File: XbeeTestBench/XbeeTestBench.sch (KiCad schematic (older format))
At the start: 7 parts, among them J1 Conn_01x02, J2 Conn_01x06, J3 Conn_01x15, J4 Conn_01x15, U1 Xbee802.15.4

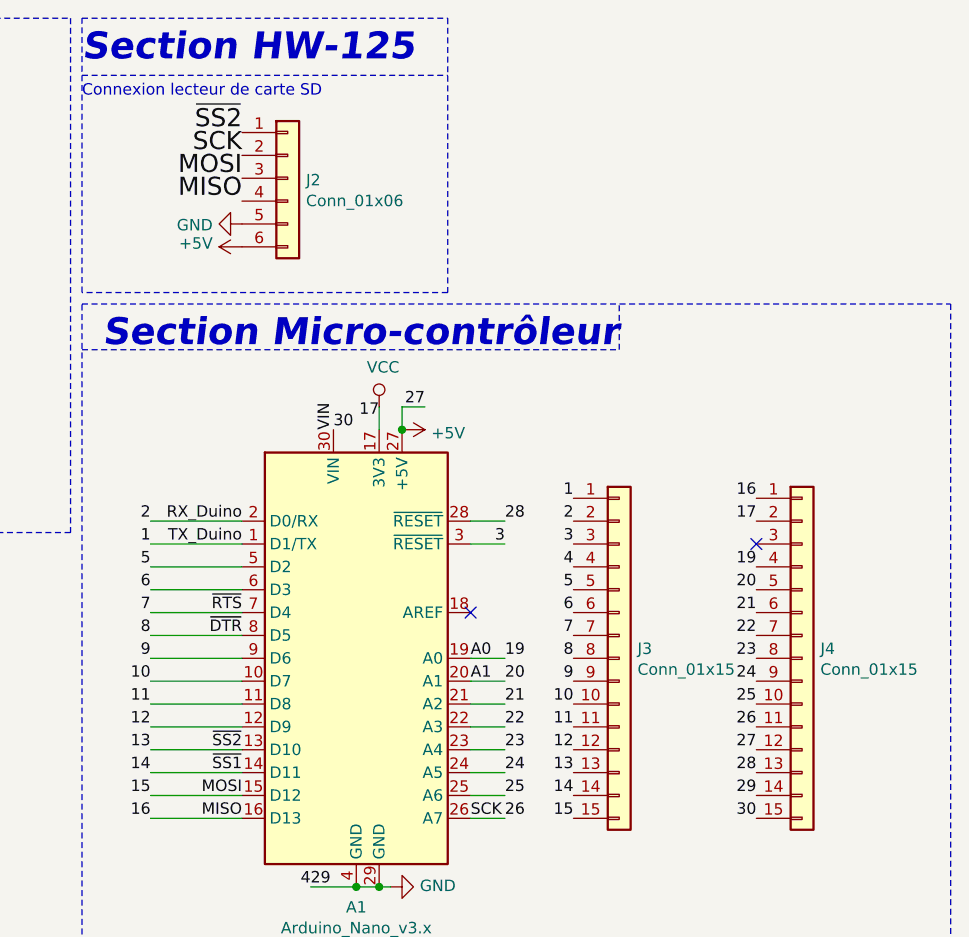
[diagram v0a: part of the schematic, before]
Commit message: Mise à jour + PDF Banc Xbee
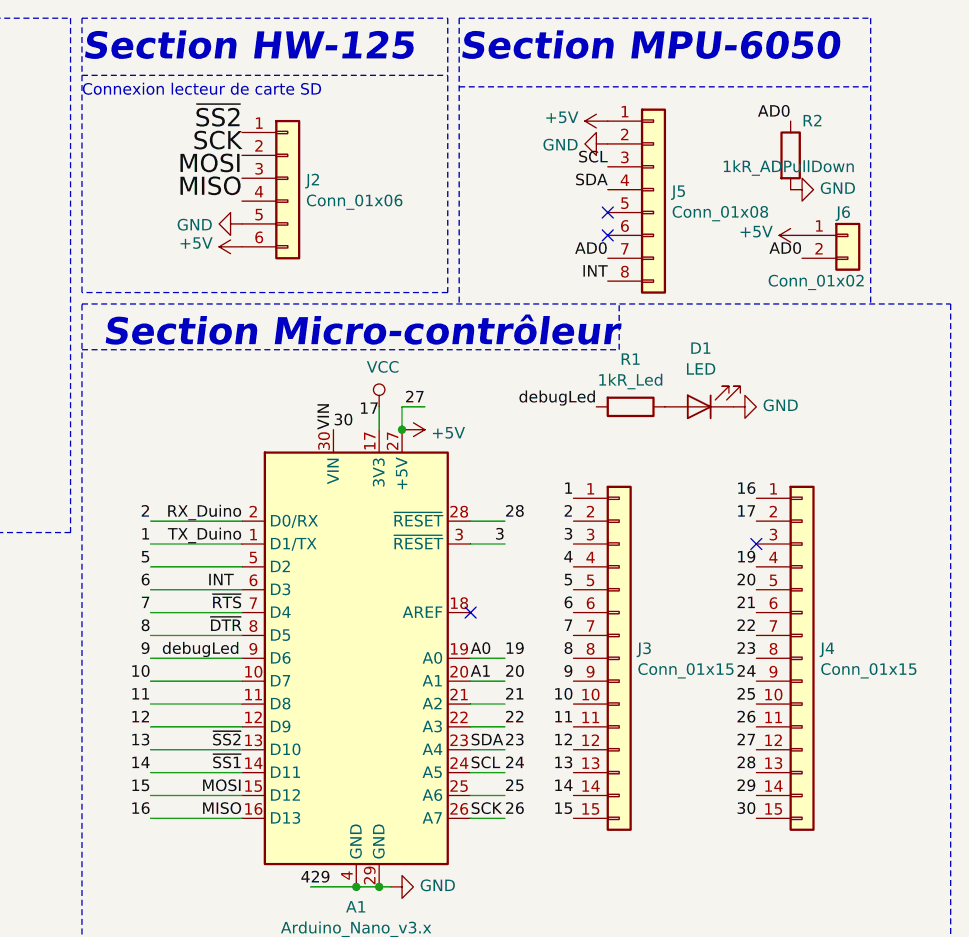
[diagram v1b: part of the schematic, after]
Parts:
- added D1: LED, LED_THT:LED_D5.0mm, symbol Device:LED
- added J5: Conn_01x08, Connector_PinSocket_2.54mm:PinSocket_1x08_P2.54mm_Vertical, symbol Connector_Generic:Conn_01x08
- added J6: Conn_01x02, Connector_PinSocket_2.54mm:PinSocket_1x02_P2.54mm_Horizontal, symbol Connector_Generic:Conn_01x02
- added R1: 1kR_Led, Resistor_SMD:R_1206_3216Metric_Pad1.42x1.75mm_HandSolder, symbol Device:R
- added R2: 1kR_ADPullDown, Resistor_SMD:R_1206_3216Metric_Pad1.42x1.75mm_HandSolder, symbol Device:R
- J1: footprint Connector_PinHeader_2.54mm:PinHeader_1x02_P2.54mm_Vertical -> rex:BatConn
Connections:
- net +5V: now also J5.1 (Pin_1), J6.1 (Pin_1)
- net 23: now also J5.4 (Pin_4)
- net 24: now also J5.3 (Pin_3)
- net 6: now also J5.8 (Pin_8)
- net 9: now also R1.2
- net GND: now also D1.1 (K), J5.2 (Pin_2), R2.2
- new net: D1.2 (A), R1.1
- new net AD0: J5.7 (Pin_7), J6.2 (Pin_2), R2.1
- no-connect marks 10 -> 12
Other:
- note added: "Section MPU-6050\n"
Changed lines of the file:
@@
 F 0 "J1" H 1480 3392 50  0000 L CNN
 F 1 "Conn_01x02" H 1480 3301 50  0000 L CNN
-F 2 "Connector_PinHeader_2.54mm:PinHeader_1x02_P2.54mm_Vertical" H 1400 3400 50  0001 C CNN
+F 2 "rex:BatConn" H 1400 3400 50  0001 C CNN
 F 3 "~" H 1400 3400 50  0001 C CNN
 	1    1400 3400
@@
 Wire Notes Line
 	3150 4550 3150 1750
-Wire Notes Line
-	3150 1750 6950 1750
 Text Notes 5500 1950 2    118  Italic 24
 Section Micro-contrôleur
@@
 	1    0    0    -1
 $EndComp
+$Comp
+L Connector_Generic:Conn_01x08 J5
+U 1 1 5DEA7475
+P 5650 1250
+F 0 "J5" H 5730 1242 50  0000 L CNN
+F 1 "Conn_01x08" H 5730 1151 50  0000 L CNN
+F 2 "Connector_PinSocket_2.54mm:PinSocket_1x08_P2.54mm_Vertical" H 5650 1250 50  0001 C CNN
+F 3 "~" H 5650 1250 50  0001 C CNN
+	1    5650 1250
+	1    0    0    -1
+$EndComp
+Text Label 5450 1650 2    50   ~ 0
+INT
+Text Label 5450 1550 2    50   ~ 0
+AD0
+Text Label 5450 1250 2    50   ~ 0
+SDA
+Text Label 5450 1150 2    50   ~ 0
+SCL
+$Comp
+L power:GND #PWR014
+U 1 1 5DEA9213
+P 5450 1050
+F 0 "#PWR014" H 5450 800 50  0001 C CNN
+F 1 "GND" V 5455 922 50  0000 R CNN
+F 2 "" H 5450 1050 50  0001 C CNN
+F 3 "" H 5450 1050 50  0001 C CNN
+	1    5450 1050
+	0    1    1    0
+$EndComp
+$Comp
+L power:+5V #PWR013
+U 1 1 5DEA998E
+P 5450 950
+F 0 "#PWR013" H 5450 800 50  0001 C CNN
+F 1 "+5V" V 5465 1078 50  0000 L CNN
+F 2 "" H 5450 950 50  0001 C CNN
+F 3 "" H 5450 950 50  0001 C CNN
+	1    5450 950
+	0    -1   -1   0
+$EndComp
+Text Notes 4800 700  0    118  Italic 24
+Section MPU-6050\n
+Wire Notes Line
+	4800 500  6600 500
+Wire Notes Line
+	6600 500  6600 1750
+Wire Notes Line
+	4800 800  6600 800
+Wire Notes Line
+	4800 500  4800 1750
+Wire Notes Line
+	3150 1750 6950 1750
+Text Label 4850 3700 0    50   ~ 0
+SDA
+Text Label 4850 3800 0    50   ~ 0
+SCL
+Text Label 3700 3000 0    50   ~ 0
+INT
+Text Label 6300 1550 2    50   ~ 0
+AD0
+$Comp
+L Connector_Generic:Conn_01x02 J6
+U 1 1 5DEC5912
+P 6500 1450
+F 0 "J6" H 6450 1550 50  0000 L CNN
+F 1 "Conn_01x02" H 6150 1250 50  0000 L CNN
+F 2 "Connector_PinSocket_2.54mm:PinSocket_1x02_P2.54mm_Horizontal" H 6500 1450 50  0001 C CNN
+F 3 "~" H 6500 1450 50  0001 C CNN
+	1    6500 1450
+	1    0    0    -1
+$EndComp
+$Comp
+L power:+5V #PWR017
+U 1 1 5DEC6210
+P 6300 1450
+F 0 "#PWR017" H 6300 1300 50  0001 C CNN
+F 1 "+5V" V 6315 1578 50  0000 L CNN
+F 2 "" H 6300 1450 50  0001 C CNN
+F 3 "" H 6300 1450 50  0001 C CNN
+	1    6300 1450
+	0    -1   -1   0
+$EndComp
+$Comp
+L Device:R R2
+U 1 1 5DEC689E
+P 6250 1100
+F 0 "R2" H 6300 1250 50  0000 L CNN
+F 1 "1kR_ADPullDown" H 5950 1050 50  0000 L CNN
+F 2 "Resistor_SMD:R_1206_3216Metric_Pad1.42x1.75mm_HandSolder" V 6180 1100 50  0001 C CNN
+F 3 "~" H 6250 1100 50  0001 C CNN
+	1    6250 1100
+	1    0    0    -1
+$EndComp
+Text Label 6250 950  2    50   ~ 0
+AD0
+$Comp
+L power:GND #PWR016
+U 1 1 5DEC72B3
+P 6250 1250
+F 0 "#PWR016" H 6250 1000 50  0001 C CNN
+F 1 "GND" V 6255 1122 50  0000 R CNN
+F 2 "" H 6250 1250 50  0001 C CNN
+F 3 "" H 6250 1250 50  0001 C CNN
+	1    6250 1250
+	0    -1   -1   0
+$EndComp
+Text Label 3500 3300 0    50   ~ 0
+debugLed
+Text Label 5400 2200 2    50   ~ 0
+debugLed
+$Comp
+L Device:LED D1
+U 1 1 5DEC9C8F
+P 5850 2200
+F 0 "D1" H 5843 1945 50  0000 C CNN
+F 1 "LED" H 5843 2036 50  0000 C CNN
+F 2 "LED_THT:LED_D5.0mm" H 5850 2200 50  0001 C CNN
+F 3 "~" H 5850 2200 50  0001 C CNN
+	1    5850 2200
+	-1   0    0    1
+$EndComp
+$Comp
+L power:GND #PWR015
+U 1 1 5DECA5E3
+P 6000 2200
+F 0 "#PWR015" H 6000 1950 50  0001 C CNN
+F 1 "GND" V 6005 2072 50  0000 R CNN
+F 2 "" H 6000 2200 50  0001 C CNN
+F 3 "" H 6000 2200 50  0001 C CNN
+	1    6000 2200
+	0    -1   -1   0
+$EndComp
+$Comp
+L Device:R R1
+U 1 1 5DECC8B0
+P 5550 2200
+F 0 "R1" V 5343 2200 50  0000 C CNN
+F 1 "1kR_Led" V 5434 2200 50  0000 C CNN
+F 2 "Resistor_SMD:R_1206_3216Metric_Pad1.42x1.75mm_HandSolder" V 5480 2200 50  0001 C CNN
+F 3 "~" H 5550 2200 50  0001 C CNN
+	1    5550 2200
+	0    1    1    0
+$EndComp
+NoConn ~ 5450 1450
+NoConn ~ 5450 1350
 $EndSCHEMATC
